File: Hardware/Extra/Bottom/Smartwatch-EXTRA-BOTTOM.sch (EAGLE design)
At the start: 37 parts, among them U1 AD5242-SO16, U3 PCF8523

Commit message: Extra features updated
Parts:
- removed C19: 2.2n, LinnesLab-Passives:CAPACITOR0603
- removed C20: 22u, LinnesLab-Passives:CAPACITOR0603
- removed R23: 1M, LinnesLab-Passives:RESISTOR0603
- removed R24: 10k, LinnesLab-Passives:RESISTOR0603
- added C3, C4: 100n, LinnesLab-Passives:CAPACITOR0603
- added J2: (no value), LinnesLab-Connectors:CONN_02.50MIL
- added R1, R2: 10k, LinnesLab-Passives:RESISTOR0603
- C10: value 100n -> 2.2n
- C11: value 100n -> 22u
- J1: device LinnesLab-Connectors:CONN_07 -> LinnesLab-Connectors:CONN_07-1.27MM
- R13: value 220k -> 1M
- R14: value 10M -> 10k
- R3: value 10k -> 220k
- R4: value 10k -> 10M
- renumbered C14 to C5, C15 to C6, C16 to C7, C17 to C8, C18 to C9, C21 to C12, C22 to C13, R15 to R5, R16 to R6, R17 to R7, R18 to R8, R19 to R9, R20 to R10, R21 to R11, R22 to R12, U$3 to U2, U$4 to U4, XTAL2 to XTAL1
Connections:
- net 3.3V: now also C4.2, R1.2, R2.2; no longer C11.2, R13.2, R4.2
- net A6/TIA: now also C3.2; no longer C10.2
- net G.W2: now also R14.1; no longer R24.1
- net GND: now also C4.1; no longer C11.1
- net N$13: now also R3.1; no longer R13.1
- net N$15: now also R4.1; no longer R14.1
- net N$16: now also R4.2; no longer R14.2
- net N$18: now also C10.2, R13.2; no longer C19.2, R23.2
- net N$19: now also C10.1, C11.1; no longer C19.1, C20.1
- net N$20: now also C11.2, R14.2; no longer C20.2, R24.2
- net PD.C: now also C3.1; no longer C10.1
- net SCL: now also R1.1; no longer R3.1
- net SDA: now also R2.1; no longer R4.1
- net VREF: now also R13.1; no longer R23.1
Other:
- moved on the sheet: C10, C11, R13, R14, R3, R4

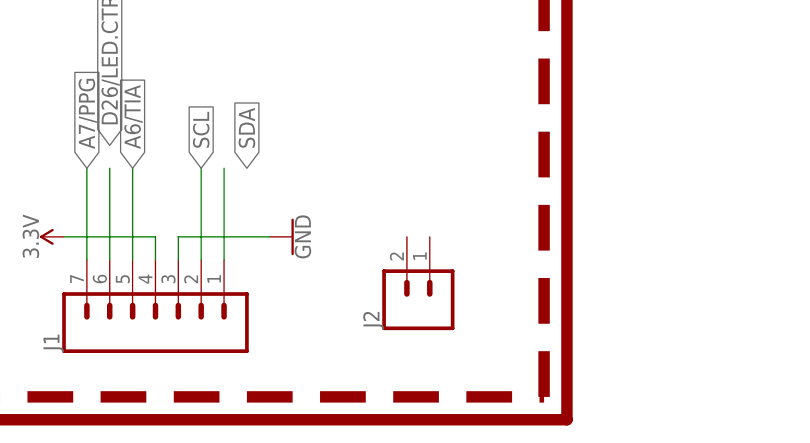
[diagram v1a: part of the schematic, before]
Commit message: Extra Silkscreens updated
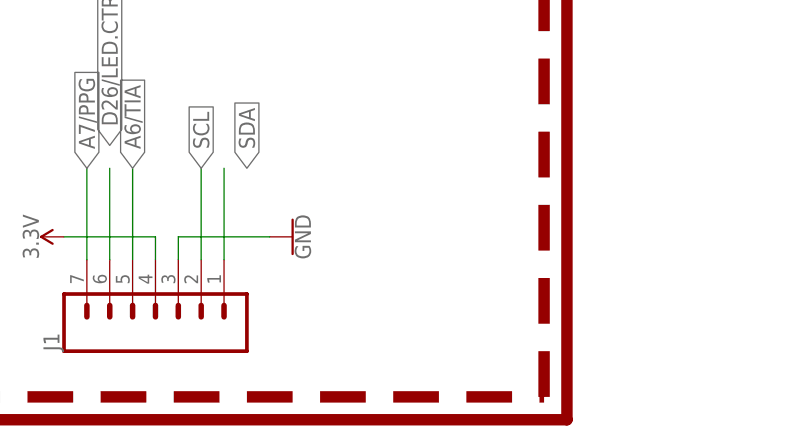
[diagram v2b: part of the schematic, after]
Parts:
- removed J2: (no value), LinnesLab-Connectors:CONN_02.50MIL
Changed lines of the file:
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@@
 <part name="GND6" library="LinnesLab-Symbols" deviceset="GND" device=""/>
 <part name="SUPPLY1" library="LinnesLab-Symbols" deviceset="3.3V" device=""/>
-<part name="J2" library="LinnesLab-Connectors" deviceset="CONN_02" device=".50MIL"/>
 </parts>
 <sheets>
@@
 <attribute name="VALUE" x="147.066" y="-25.4" size="1.778" layer="96" rot="R90" align="bottom-center"/>
 </instance>
-<instance part="J2" gate="G$1" x="190.5" y="-33.02" smashed="yes" rot="R90">
-<attribute name="VALUE" x="195.326" y="-35.56" size="1.778" layer="96" font="vector" rot="R90"/>
-<attribute name="NAME" x="184.912" y="-35.56" size="1.778" layer="95" font="vector" rot="R90"/>
-</instance>
 </instances>

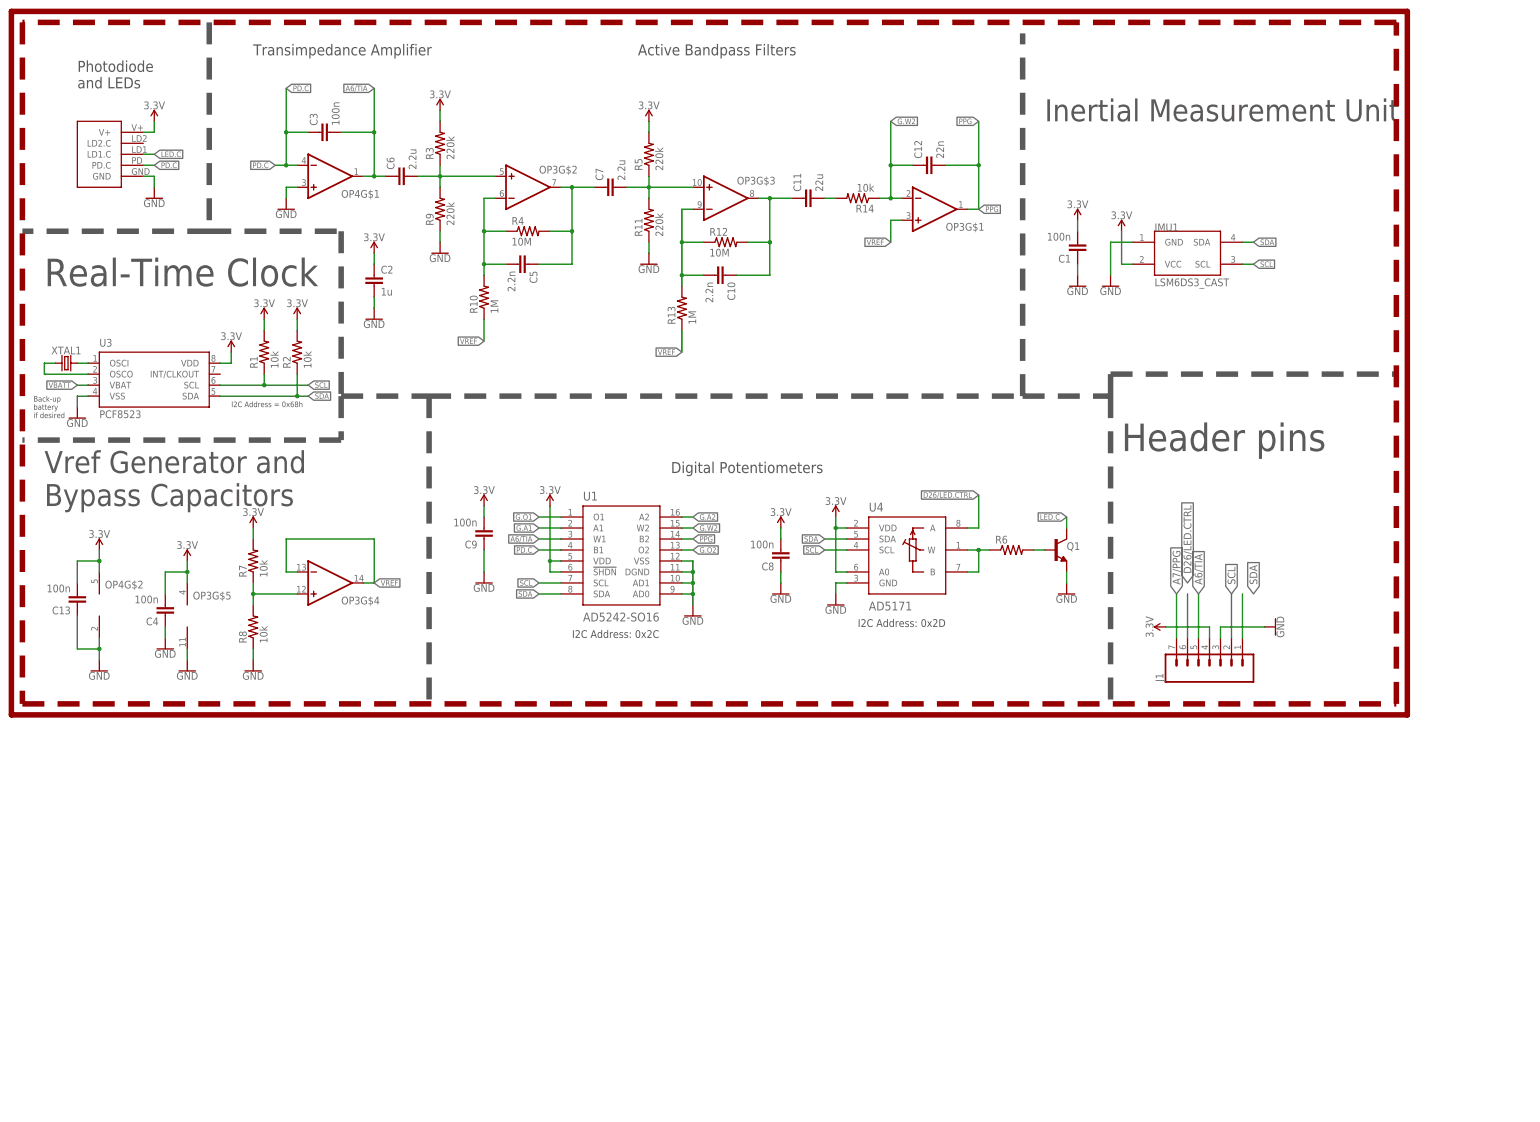
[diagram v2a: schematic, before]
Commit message: Encoder Added, Silkscreen Updated, Bom Updated
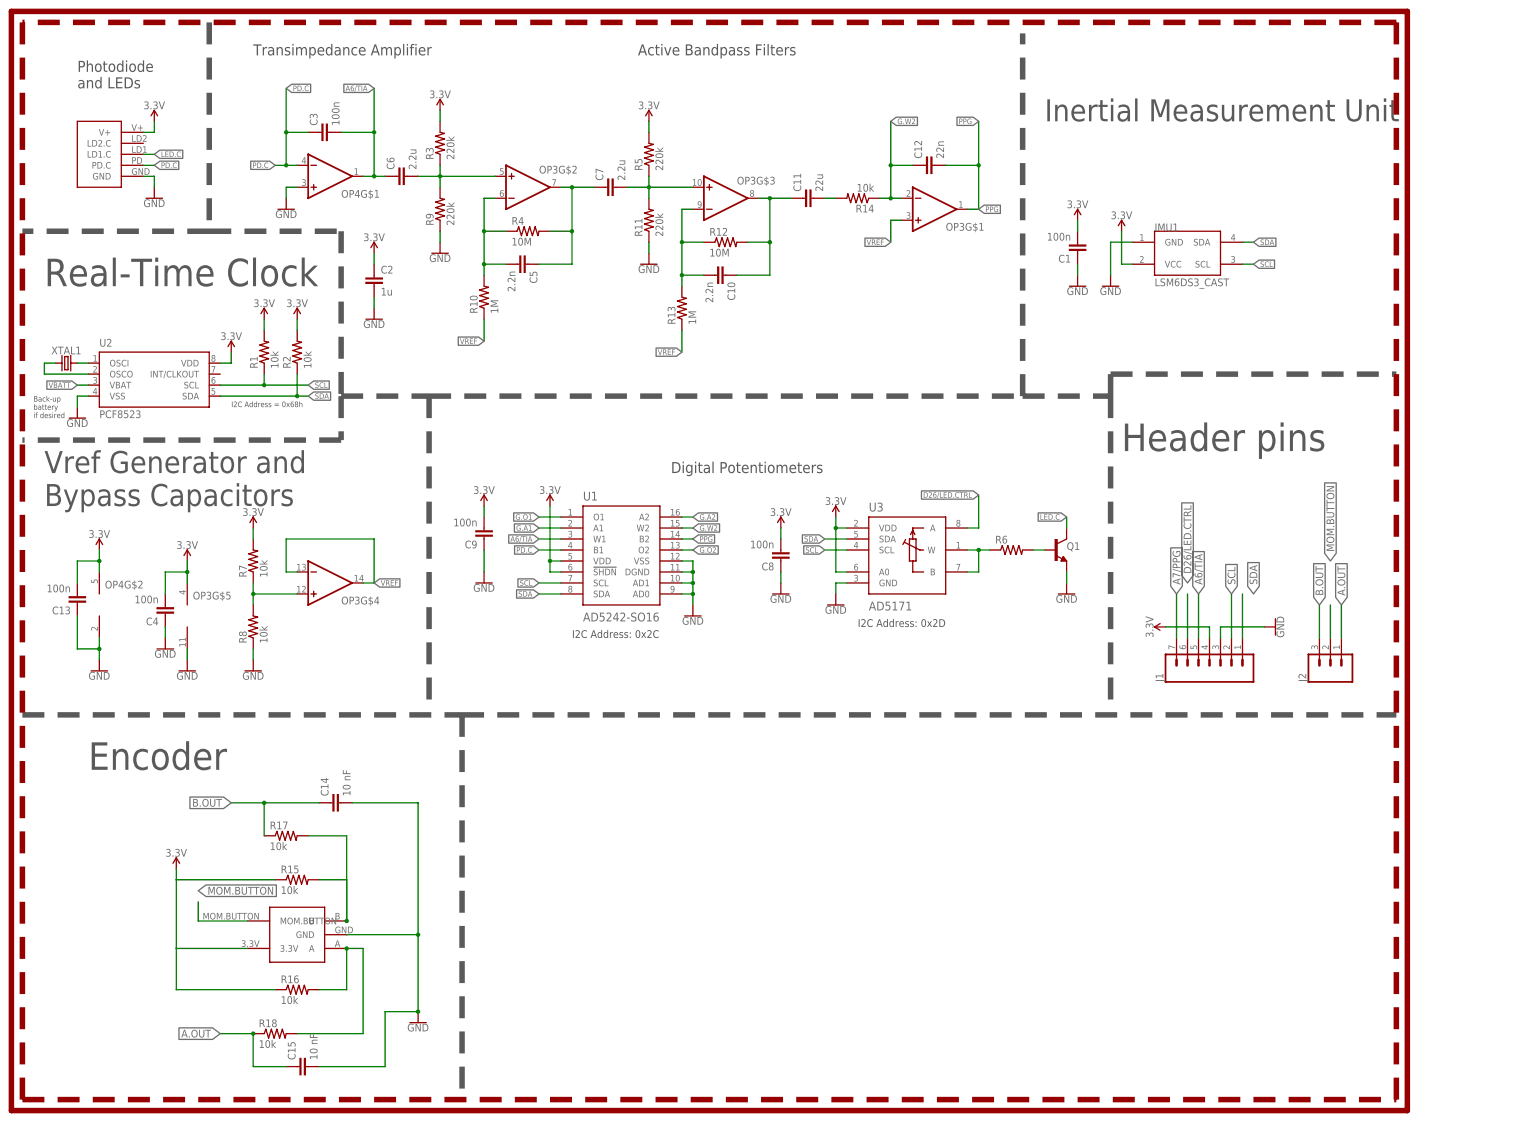
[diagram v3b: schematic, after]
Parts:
- added C14, C15: 10 nF, LinnesLab-Passives:CAPACITOR0603
- added ENC1: PEC09-2220F-S0012, Encoder:PEC09-2220F-S0012
- added J2: (no value), LinnesLab-Connectors:CONN_03.50MIL
- added R15, R16, R17, R18: 10k, LinnesLab-Passives:RESISTOR0603
- U2: value (none) -> PCF8523; device LinnesLab-Connectors:PPG.MODULE.2 -> LinnesLab-Clocks:PCF8523; DIGIKEY (none) -> 568-5306-1-ND; I2C_ADDRESS (none) -> 0x68h; MFN (none) -> PCF8523T/1,118; MFN_MANUFACTURER (none) -> NXP USA Inc.
- U3: value PCF8523 -> AD5171; device LinnesLab-Clocks:PCF8523 -> LinnesLab-DigitalIC:AD5171; DIGIKEY 568-5306-1-ND -> (none); I2C_ADDRESS 0x68h -> (none); MFN PCF8523T/1,118 -> (none); MFN_MANUFACTURER NXP USA Inc. -> (none)
- U4: value AD5171 -> (none); device LinnesLab-DigitalIC:AD5171 -> LinnesLab-Connectors:PPG.MODULE.2
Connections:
- new net A.OUT: C15.1, J2.1, R18.1
- new net B.OUT: C14.1, J2.3, R17.1
- new net MOM.BUTTON: ENC1.MOM.BUTTON, J2.2
- new net N$1: ENC1.A, R16.2, R18.2
- new net N$4: ENC1.B, R15.2, R17.2
- net 3.3V: now also ENC1.3.3V, R15.1, R16.1, U2.VDD, U3.A0, U4.V+; no longer U2.V+, U4.A0, U4.VDD
- net D26/LED.CTRL: now also U3.A; no longer U4.A
- net GND: now also C14.2, C15.2, ENC1.GND, U2.VSS, U3.GND; no longer U2.GND, U3.VSS
- net LED.C: now also U4.LD1.C; no longer U2.LD1.C
- net N$2: now also U2.OSCO; no longer U3.OSCO
- net N$3: now also U2.OSCI; no longer U3.OSCI
- net N$9: now also U3.B, U3.W; no longer U4.B, U4.W
- net PD.C: now also U4.PD.C; no longer U2.PD.C
- net SCL: now also U2.SCL; no longer U4.SCL
- net SDA: now also U2.SDA; no longer U4.SDA
- net VBATT: now also U2.VBAT; no longer U3.VBAT
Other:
- note added: "Encoder"

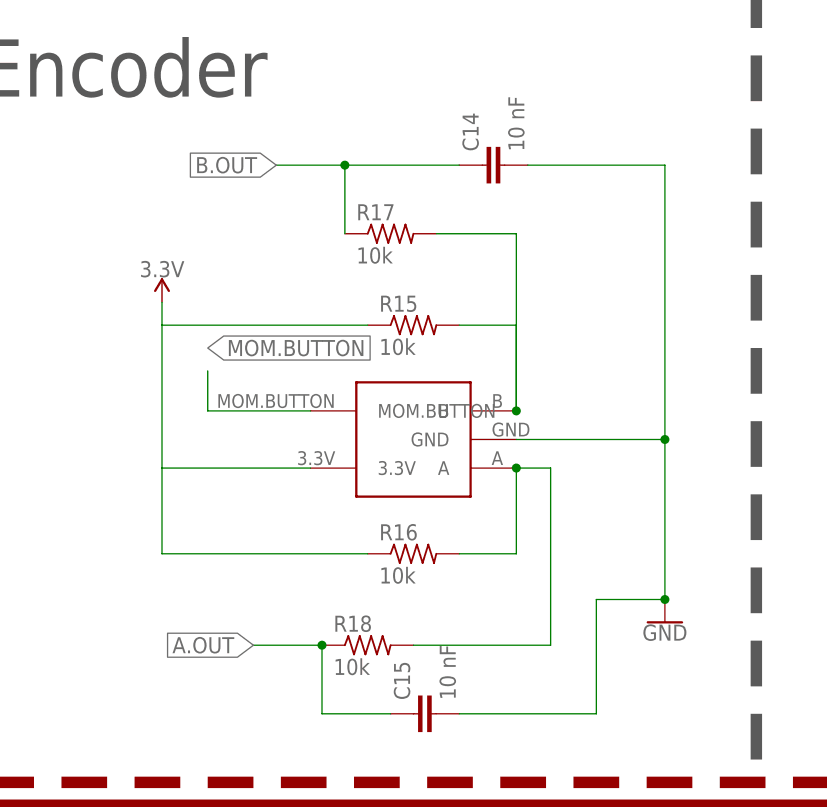
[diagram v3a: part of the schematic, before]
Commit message: Encoder changed, BOMs updated
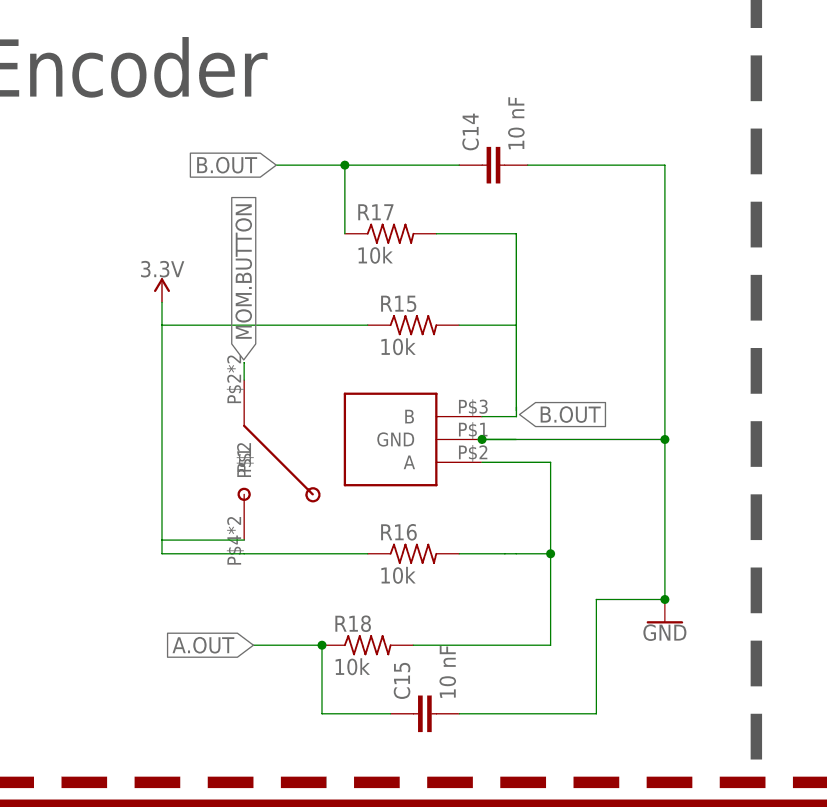
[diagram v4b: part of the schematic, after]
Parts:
- added B1: SWITCH, Encoder:SWITCH
- ENC1: value PEC09-2220F-S0012 -> EVQVU; device Encoder:PEC09-2220F-S0012 -> Encoder:EVQVU
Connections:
- removed net N$1: ENC1.A, R16.2, R18.2
- net 3.3V: now also B1.P$2; no longer ENC1.3.3V
- net A.OUT: now also ENC1.A, R16.2, R18.2
- net B.OUT: now also ENC1.B
- net MOM.BUTTON: now also B1.P$1; no longer ENC1.MOM.BUTTON
- net N$4: no longer ENC1.B

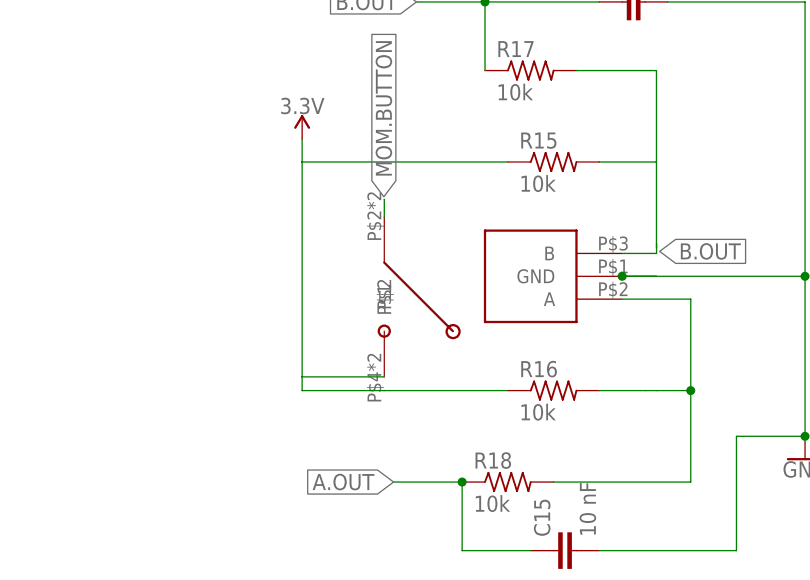
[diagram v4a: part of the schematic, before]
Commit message: GPS Removed, added back original display, kept pads for adafruit display
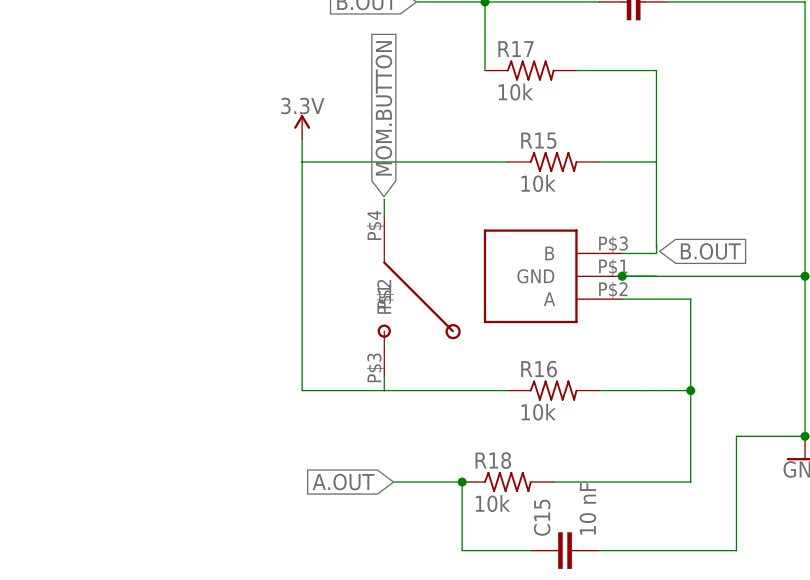
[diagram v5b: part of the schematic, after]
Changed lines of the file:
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@@
 <pinref part="SUPPLY2" gate="G$1" pin="3.3V"/>
 <pinref part="R15" gate="G$1" pin="1"/>
-<wire x1="-78.74" y1="-109.22" x2="-78.74" y2="-107.696" width="0.1524" layer="91"/>
-<wire x1="-78.74" y1="-107.696" x2="-78.74" y2="-83.82" width="0.1524" layer="91"/>
+<wire x1="-78.74" y1="-109.22" x2="-78.74" y2="-83.82" width="0.1524" layer="91"/>
 <wire x1="-78.74" y1="-83.82" x2="-78.74" y2="-81.28" width="0.1524" layer="91"/>
 <wire x1="-78.74" y1="-83.82" x2="-55.88" y2="-83.82" width="0.1524" layer="91"/>
 <pinref part="R16" gate="G$1" pin="1"/>
-<wire x1="-78.74" y1="-109.22" x2="-55.88" y2="-109.22" width="0.1524" layer="91"/>
+<wire x1="-78.74" y1="-109.22" x2="-69.611240625" y2="-109.22" width="0.1524" layer="91"/>
 <pinref part="B1" gate="G$1" pin="P$2"/>
-<wire x1="-69.611240625" y1="-107.696" x2="-78.74" y2="-107.696" width="0.1524" layer="91"/>
+<wire x1="-68.58" y1="-109.22" x2="-55.88" y2="-109.22" width="0.1524" layer="91"/>
+<wire x1="-69.611240625" y1="-107.696" x2="-69.611240625" y2="-109.22" width="0.1524" layer="91"/>
+<wire x1="-69.611240625" y1="-109.22" x2="-68.58" y2="-109.22" width="0.1524" layer="91"/>
 </segment>
 </net>
